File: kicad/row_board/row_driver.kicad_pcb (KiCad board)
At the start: 2 copper layers, 100 x 100 mm, 86 parts, among them J1 Panel row connector (female), J2 Row daisy chain connector (ma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, J3 Conn_01x04, J4 Conn_02x05_Odd_Even, J5 Conn_01x10, J6 Barrel_Jack, Q1 2N3904, U1 TPIC6B595, U10 TXB0108-PWR, U11 AdafruitProTrinket5V, U2 TPIC6B595, U3 TBD62783, U4 TPIC6B595, U5 TPIC6B595, U6 TBD62783, U7 WE-FDSM_DC/DC_5V, U8 4N25, U9 WeMos_mini

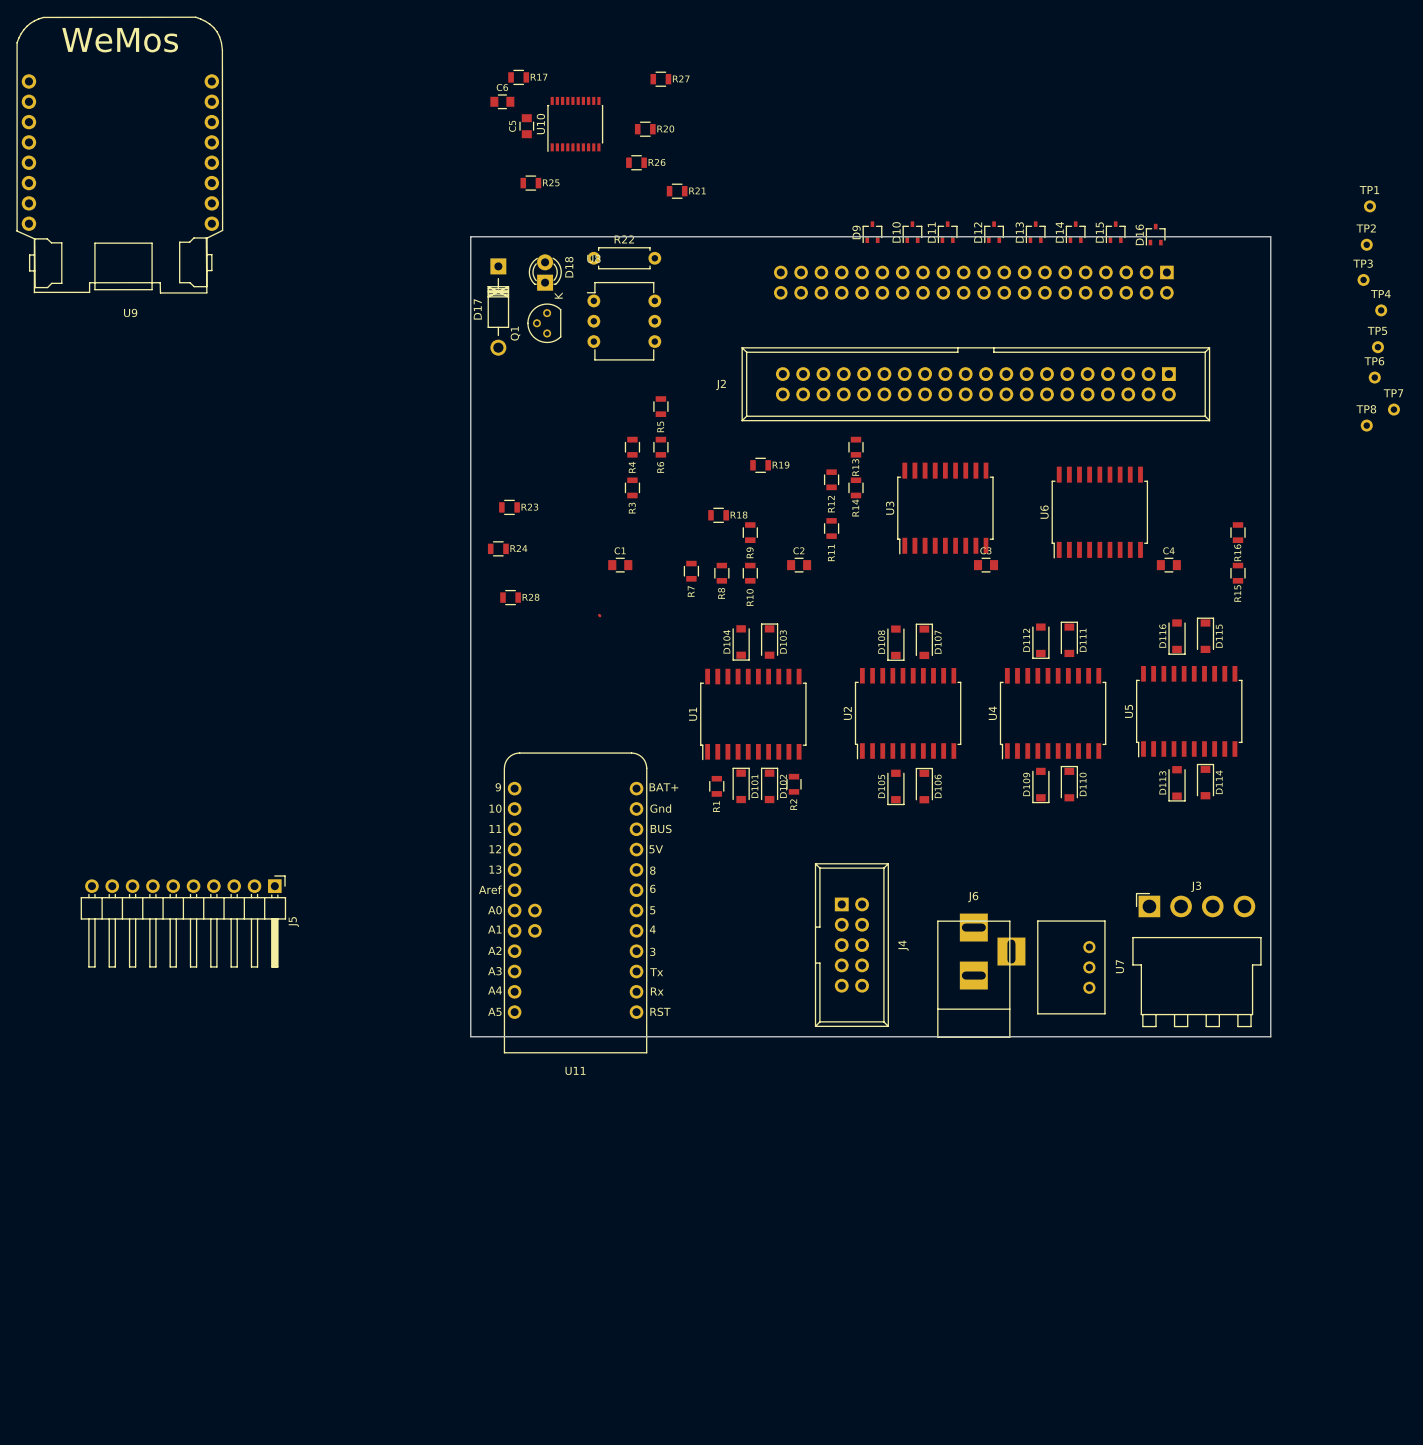
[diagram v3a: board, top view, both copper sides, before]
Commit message: Combine two controllers
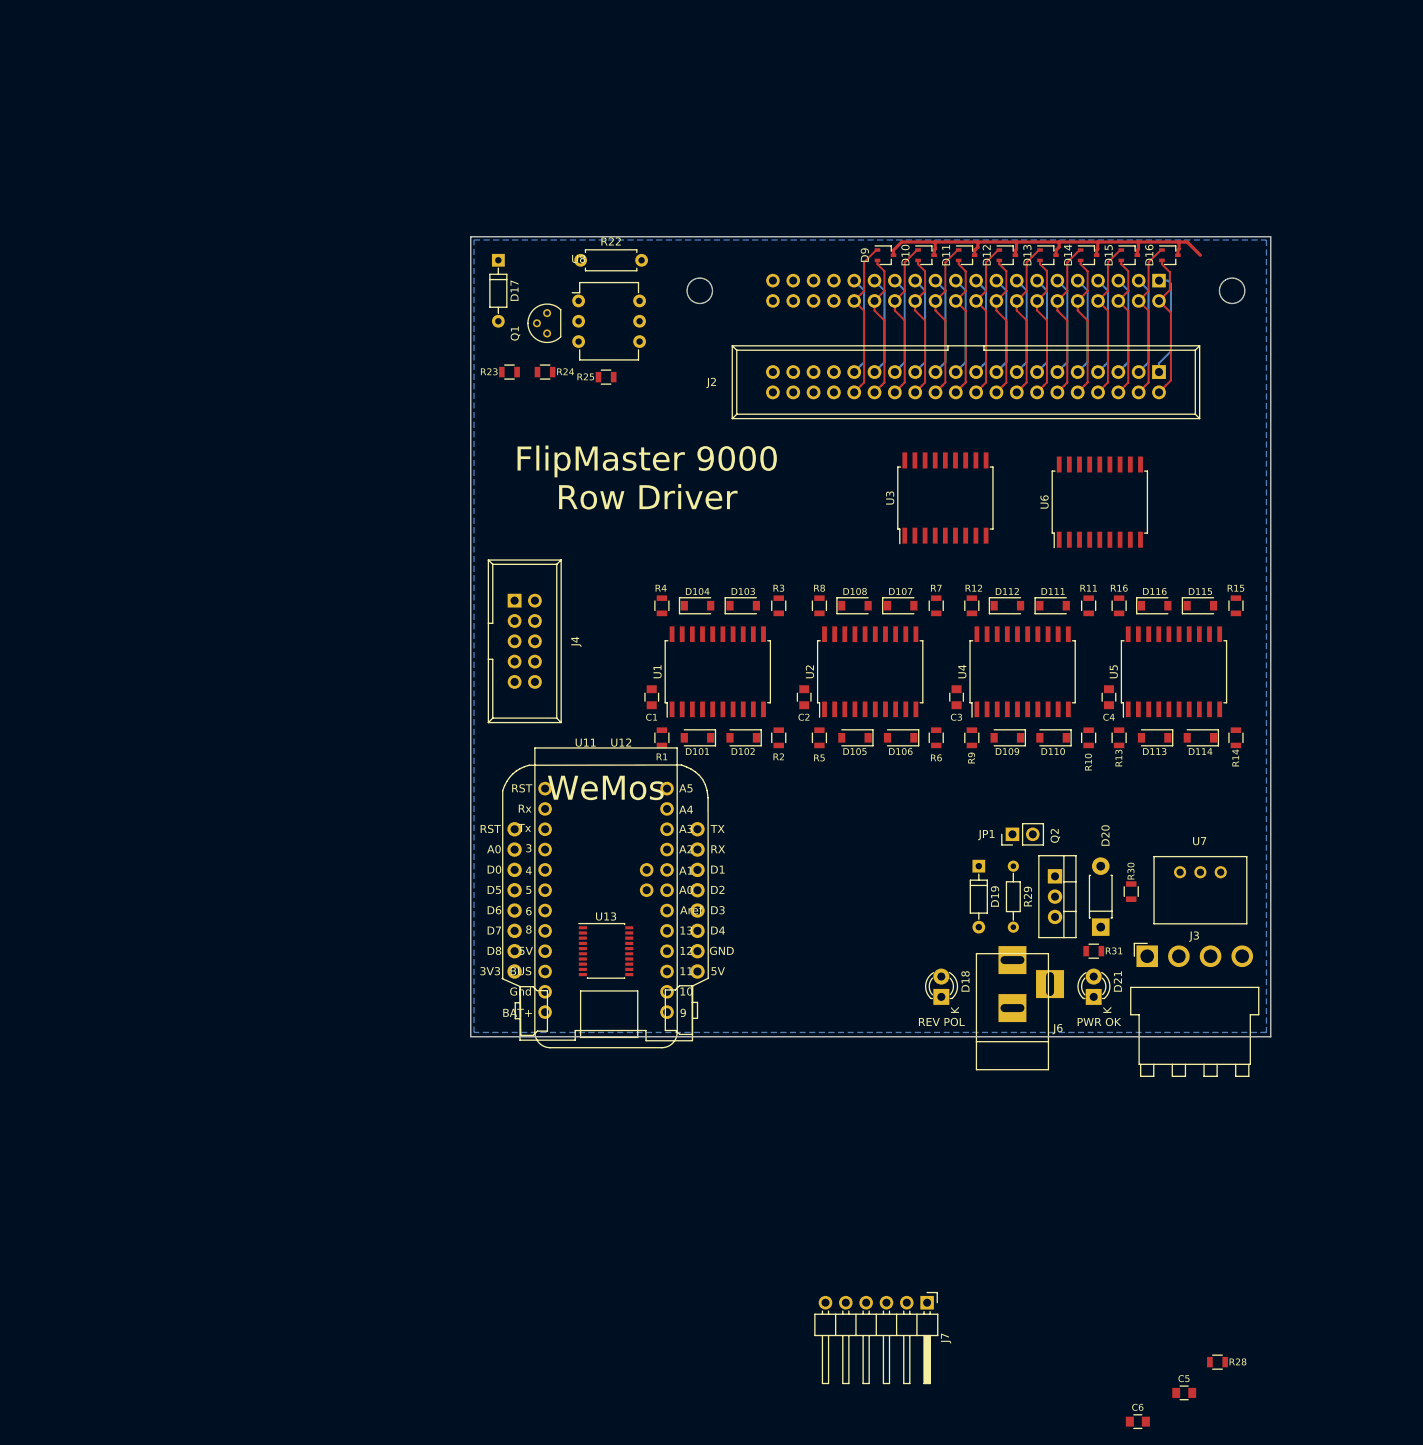
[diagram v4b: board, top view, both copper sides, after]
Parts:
- removed J5: Conn_01x10, Pin_Headers:Pin_Header_Angled_1x10_Pitch2.54mm
- removed R17, R18, R19, R20, R26, R27: 68K, lib_fp:R_0805
- removed R21: 10K, lib_fp:R_0805
- removed TP1, TP2, TP3, TP4, TP5, TP6, TP7, TP8: TEST_1P, Measurement_Points:Measurement_Point_Round-TH_Small
- removed U10: TXB0108-PWR, Housings_SSOP:SSOP-20_4.4x6.5mm_Pitch0.65mm
- removed U9: WeMos_mini, wemos_d1_mini:D1_mini_can_up
- added D19: 1N4148, Diodes_THT:D_DO-35_SOD27_P7.62mm_Horizontal, F.Cu at (88.5, 103.7)
- added D20: 1N4742, Diodes_THT:D_DO-41_SOD81_P7.62mm_Horizontal, F.Cu at (103.7, 111.3)
- added D21: LED, LEDs:LED-3MM, F.Cu at (102.9, 120.0)
- added J7: Conn_01x06, Pin_Headers:Pin_Header_Angled_1x06_Pitch2.54mm, F.Cu at (82.0, 158.2)
- added JP1: Jumper, Pin_Headers:Pin_Header_Straight_1x02_Pitch2.54mm, F.Cu at (92.7, 99.7)
- added Q2: FQP47P06, TO_SOT_Packages_THT:TO-220_Vertical, F.Cu at (98.0, 104.9)
- added R29: 2K7, Resistors_THT:R_Axial_DIN0204_L3.6mm_D1.6mm_P7.62mm_Horizontal, F.Cu at (92.8, 103.7)
- added R30: 2K7, lib_fp:R_0805, F.Cu at (107.6, 106.8)
- added R31: 470, lib_fp:R_0805, F.Cu at (102.9, 114.3)
- added U12: WeMos_mini, wemos_d1_mini:D1_mini_can_up, F.Cu at (41.9, 109.2)
- added U13: TXB0108-PWR, Housings_SSOP:SSOP-20_4.4x6.5mm_Pitch0.65mm, F.Cu at (41.9, 114.3)
- D17: value D -> 1N4148; footprint Diodes_THT:Diode_DO-41_SOD81_Horizontal_RM10 -> Diodes_THT:D_DO-35_SOD27_P7.62mm_Horizontal
- J1: footprint Socket_Strips:Socket_Strip_Straight_2x20_Pitch2.54mm -> lib_fp:Socket_Strip_Straight_2x20_Pitch2.54mm
- R23: value 4K7 -> 1K
- R28: value 2K7 -> 470
- moved C6 183.1 mm to (108.4, 173.1)
- moved C5 178.4 mm to (114.2, 169.5), turned to 0 degrees
- moved R28 130.2 mm to (118.3, 165.7)
- moved D18 102.1 mm to (83.8, 120.0)
- moved R14 56.9 mm to (120.7, 87.6)
- moved J4 55.8 mm to (30.5, 70.5)
- moved R6 50.0 mm to (83.2, 87.6)
- moved R13 49.0 mm to (106.0, 87.6)
- moved R10 47.0 mm to (102.2, 87.6)
- moved R5 45.9 mm to (68.6, 87.6)
- moved R9 37.7 mm to (87.6, 87.6)
- moved R11 33.5 mm to (102.2, 71.1)
- moved R7 30.9 mm to (83.2, 71.1)
- moved R25 26.0 mm to (41.9, 42.5), turned to 180 degrees
- moved J1 25.2 mm to (86.9, 31.8), turned to 0 degrees
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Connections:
- D18 pad 2: Net-(D18-Pad2) -> GND
- J3 pad 3: Net-(J3-Pad3) -> +24V
- J4 pad 5: COL_SR_CLK -> RC_SHIFT_CLK
- J4 pad 7: RC_REG_CLK -> COL_REG_CLK
- J4 pad 9: ~RC_CLR -> ~RC_CLEAR
- J6 pad 1: +24V -> Net-(J6-Pad1)
- Q1 pad 3: Net-(D18-Pad1) -> Net-(Q1-Pad3)
- R22 pad 2: ROW1_L -> ROW16_L
- R25 pad 1: +3V3 -> +5V
- U1 pad 12: RC_REG_CLK -> ROW_REG_CLK
- U1 pad 13: ROW_SR_CLK -> RC_SHIFT_CLK
- U1 pad 8: ~RC_CLR -> ~RC_CLEAR
- U11 pad 1: Net-(U11-Pad1) -> SENSE_EN
- U11 pad 10: Net-(U11-Pad10) -> CTRL3
- U11 pad 11: Net-(U11-Pad11) -> CTRL4
- U11 pad 12: Net-(U11-Pad12) -> CTRL5
- U11 pad 16: Net-(U11-Pad16) -> ~ROW_EN
- U11 pad 17: Net-(U11-Pad17) -> ROW_REG_CLK
- U11 pad 18: Net-(U11-Pad18) -> ~COL_EN
- U11 pad 19: Net-(U11-Pad19) -> COL_REG_CLK
- U11 pad 20: Net-(U11-Pad20) -> ~RC_CLEAR
- U11 pad 21: Net-(U11-Pad21) -> +5V
- U11 pad 23: Net-(U11-Pad23) -> GND
- U11 pad 3: Net-(U11-Pad3) -> RC_DATA
- U11 pad 4: Net-(U11-Pad4) -> ~SENSE
- U11 pad 5: Net-(U11-Pad5) -> RC_SHIFT_CLK
- U11 pad 7: Net-(U11-Pad7) -> CTRL0
- U11 pad 8: Net-(U11-Pad8) -> CTRL1
- U11 pad 9: Net-(U11-Pad9) -> CTRL2
- U2 pad 12: RC_REG_CLK -> ROW_REG_CLK
- U2 pad 13: ROW_SR_CLK -> RC_SHIFT_CLK
- U2 pad 8: ~RC_CLR -> ~RC_CLEAR
- U4 pad 12: RC_REG_CLK -> ROW_REG_CLK
- U4 pad 13: ROW_SR_CLK -> RC_SHIFT_CLK
- U4 pad 8: ~RC_CLR -> ~RC_CLEAR
- U5 pad 12: RC_REG_CLK -> ROW_REG_CLK
- U5 pad 13: ROW_SR_CLK -> RC_SHIFT_CLK
- U5 pad 8: ~RC_CLR -> ~RC_CLEAR
- U8 pad 2: Net-(D18-Pad2) -> Net-(Q1-Pad3)
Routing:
- net +24V: track 0.00 -> 52.3 mm
- net ROW14_L: track 0.00 -> 20.1 mm
- net ROW12_L: track 0.00 -> 20.1 mm
- net ROW10_L: track 0.00 -> 20.1 mm
- net ROW16_L: track 0.00 -> 20.1 mm
- net ROW8_L: track 0.00 -> 20.1 mm
- net ROW6_L: track 0.00 -> 20.1 mm
- net ROW4_L: track 0.00 -> 20.1 mm
- net ROW2_L: track 0.00 -> 20.1 mm
- net ROW1_L: track 0.00 -> 18.8 mm
- net ROW7_L: track 0.00 -> 18.4 mm
- net ROW5_L: track 0.00 -> 18.4 mm
- net ROW3_L: track 0.00 -> 18.4 mm
- net ROW15_L: track 0.00 -> 18.4 mm
- net ROW9_L: track 0.00 -> 18.4 mm
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- added copper zone on B.Cu, net GND
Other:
- net class High Current: trace_width 0.35 -> 0.4; via_dia 1.2 -> 1.5; via_drill 0.7 -> 0.75
- rule trace_min: 0.127 -> 0.09
- rule via_min_drill: 0.3 -> 0.2
- rule via_min_size: 0.6 -> 0.45
- board text added: "FlipMaster 9000 Row Driver"
- board text added: "PWR OK"
- board text added: "REV POL"

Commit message: Routed shift registers and row connectors
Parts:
- C5, C6, U13: moved to B.Cu
- U12: footprint wemos_d1_mini:D1_mini_can_up -> lib_fp:D1_mini_can_up
- moved C5 103.6 mm to (31.8, 106.7), turned to 180 degrees
- moved C6 99.8 mm to (31.8, 109.2)
- moved R28 51.3 mm to (77.1, 135.2)
- moved J7 38.6 mm to (78.0, 119.9)
- moved J4 12.8 mm to (32.3, 83.2), turned to 90 degrees
- moved U7 8.28 mm to (115.6, 98.4)
- moved R23 8.14 mm to (34.9, 48.3), turned to 0 degrees
- moved U13 7.41 mm to (38.1, 108.0), turned to 270 degrees
- moved R25 5.75 mm to (42.5, 48.3)
- moved Q1 4.87 mm to (35.2, 41.9)
- moved U8 4.87 mm to (39.1, 37.8)
- moved D17 4.51 mm to (29.2, 32.4)
- moved R22 4.46 mm to (39.1, 32.4)
- moved J3 3.81 mm to (109.6, 111.1)
- moved R24 3.24 mm to (34.9, 45.1)
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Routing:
- net +5V: track 0.00 -> 264.3 mm, vias 0 -> 9
- net +24V: track 52.3 -> 172.9 mm, vias 0 -> 3
- net ~RC_CLEAR: track 0.00 -> 99.1 mm, vias 0 -> 8
- net ROW_REG_CLK: track 0.00 -> 87.9 mm, vias 0 -> 6
- net ~ROW_EN: track 0.00 -> 85.3 mm
- net RC_SHIFT_CLK: track 0.00 -> 82.4 mm
- net Net-(D102-Pad2): track 0.00 -> 75.4 mm, vias 0 -> 2
- net ROW16_L: track 20.1 -> 94.1 mm, vias 0 -> 2
- net ROW11_L: track 18.4 -> 79.9 mm, vias 0 -> 4
- net ROW15_L: track 18.4 -> 78.7 mm, vias 0 -> 2
- net ROW13_L: track 18.4 -> 77.2 mm, vias 0 -> 2
- net Net-(D101-Pad2): track 0.00 -> 54.1 mm, vias 0 -> 2
- net Net-(D104-Pad2): track 0.00 -> 50.8 mm
- net ROW3_L: track 18.4 -> 68.8 mm, vias 0 -> 2
- net ROW4_L: track 20.1 -> 68.6 mm, vias 0 -> 2
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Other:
- net class Default: via_dia 1 -> 0.5; via_drill 0.5 -> 0.3
- net class High Current: via_dia 1.5 -> 0.8; via_drill 0.75 -> 0.5
- net class Power added: clearance 0.25, trace_width 0.65, via_dia 1, via_drill 0.75

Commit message: Routed all but controllers
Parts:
- added J8: Controller B, Connectors:IDC_Header_Straight_10pins, F.Cu at (85.8, 97.2)
- J4: value Conn_02x05_Odd_Even -> Column Board Connector
- J7: value Conn_01x06 -> Controller A; footprint Pin_Headers:Pin_Header_Angled_1x06_Pitch2.54mm -> Connectors:IDC_Header_Straight_10pins
- Q2: footprint TO_SOT_Packages_THT:TO-220_Vertical -> TO_SOT_Packages_THT:TO-220_Horizontal
- U11: value AdafruitProTrinket5V -> ArduinoNanoR3; footprint lib_fp:Adafruit_Trinket_Pro -> lib_fp:Arduino_Nano_R3
- moved R28 64.9 mm to (28.6, 92.1)
- moved D18 33.3 mm to (106.0, 95.2)
- moved J7 22.8 mm to (75.6, 97.2)
- moved D19 16.6 mm to (101.0, 92.7)
- moved R29 11.6 mm to (96.5, 92.7)
- moved JP1 10.8 mm to (99.7, 108.0), turned to 0 degrees
- moved D20 7.88 mm to (95.9, 111.8)
- moved J4 7.62 mm to (32.4, 75.6)
- moved R30 6.26 mm to (105.4, 101.0), turned to 180 degrees
- moved Q2 5.34 mm to (103.4, 105.4)
- moved J3 5.08 mm to (109.6, 116.2)
- moved C5 4.67 mm to (36.4, 106.0)
- moved C6 4.67 mm to (36.4, 108.6)
- moved U13 4.67 mm to (42.7, 107.3)
- moved U11 3.13 mm to (47.8, 107.3)
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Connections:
- net RC_DATA_OUT renamed Net-(U5-Pad18)
- J7 pad 1: CTRL5 -> CTRL_A0
- J7 pad 2: CTRL4 -> GND
- J7 pad 3: CTRL3 -> CTRL_A1
- J7 pad 4: CTRL2 -> GND
- J7 pad 5: CTRL1 -> CTRL_A2
- J7 pad 6: CTRL0 -> GND
- U11 pad 1: SENSE_EN -> RC_SHIFT_CLK
- U11 pad 10: CTRL3 -> CTRL_A4
- U11 pad 11: CTRL4 -> CTRL_B4
- U11 pad 12: CTRL5 -> +5V
- U11 pad 14: Net-(U11-Pad14) -> GND
- U11 pad 16: ~ROW_EN -> Net-(U11-Pad16)
- U11 pad 17: ROW_REG_CLK -> Net-(U11-Pad17)
- U11 pad 18: ~COL_EN -> Net-(U11-Pad18)
- U11 pad 19: COL_REG_CLK -> GND
- U11 pad 20: ~RC_CLEAR -> CTRL_B0
- U11 pad 21: +5V -> CTRL_A0
- U11 pad 22: Net-(U11-Pad22) -> ~ROW_EN
- U11 pad 23: GND -> ROW_REG_CLK
- U11 pad 24: Net-(U11-Pad24) -> ~COL_EN
- U11 pad 3: RC_DATA -> Net-(U11-Pad3)
- U11 pad 4: ~SENSE -> CTRL_A1
- U11 pad 5: RC_SHIFT_CLK -> CTRL_B1
- U11 pad 6: Net-(U11-Pad6) -> CTRL_A2
- U11 pad 7: CTRL0 -> CTRL_B2
- U11 pad 8: CTRL1 -> CTRL_A3
- U11 pad 9: CTRL2 -> CTRL_B3
- U12 pad 12: ~COL_EN_3v3 -> ROW_REG_CLK_3v3
- U12 pad 13: COL_REG_CLK_3v3 -> ~COL_EN_3v3
- U12 pad 14: ROW_REG_CLK_3v3 -> COL_REG_CLK_3v3
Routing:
- net +24V: track 172.9 -> 222.2 mm
- net +5V: track 264.3 -> 292.7 mm
- net Net-(J6-Pad1): track 0.00 -> 25.4 mm
- net Net-(D20-Pad2): track 0.00 -> 13.3 mm
- net Net-(D18-Pad1): track 0.00 -> 8.00 mm
- net Net-(D19-Pad1): track 0.00 -> 4.45 mm
- net Net-(D21-Pad2): track 0.00 -> 3.57 mm
- net GND: track 30.2 -> 33.0 mm, vias 18 -> 19
- net ROW13_L: track 77.2 -> 75.3 mm
- net ROW9_L: track 64.5 -> 63.9 mm
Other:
- net class PowerBus added: clearance 0.25, trace_width 1, via_dia 1.2, via_drill 0.75
- board text added: "+24V CTR POS"
- board text added: "CONT. A"
- board text added: "CONT. B"
- board text added: "Rev. 1.0 June, 2018"

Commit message: Finished routing row board; cleaning up.
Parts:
- C5, C6, U13: moved to F.Cu
- moved R28 9.13 mm to (37.6, 91.0)
- moved J4 8.03 mm to (29.8, 67.9), turned to 270 degrees
- moved C6 7.21 mm to (43.2, 106.1), turned to 90 degrees
- moved C5 6.30 mm to (30.1, 106.1), turned to 270 degrees
- moved U13 6.05 mm to (36.7, 107.4), turned to 0 degrees
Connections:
- J4 pad 3: RC_DATA -> RC_SHIFT_CLK
- J4 pad 5: RC_SHIFT_CLK -> ~RC_CLEAR
- J4 pad 7: COL_REG_CLK -> RC_DATA
- J4 pad 9: ~RC_CLEAR -> COL_REG_CLK
- U11 pad 22: ~ROW_EN -> COL_REG_CLK
- U11 pad 25: COL_REG_CLK -> ~ROW_EN
- U12 pad 3: ~SENSE_3v3 -> RC_SHIFT_CLK_3v3
- U12 pad 4: RC_SHIFT_CLK_3v3 -> ~SENSE_3v3
- U13 pad 1: ~ROW_EN_3v3 -> RC_DATA_3v3
- U13 pad 12: ~SENSE -> ~ROW_EN
- U13 pad 13: ~RC_CLEAR -> ROW_REG_CLK
- U13 pad 14: COL_REG_CLK -> ~COL_EN
- U13 pad 15: ROW_REG_CLK -> COL_REG_CLK
- U13 pad 17: RC_DATA -> ~SENSE
- U13 pad 18: ~COL_EN -> ~RC_CLEAR
- U13 pad 20: ~ROW_EN -> RC_DATA
- U13 pad 3: ~COL_EN_3v3 -> ~RC_CLR_3v3
- U13 pad 4: RC_DATA_3v3 -> ~SENSE_3v3
- U13 pad 6: ROW_REG_CLK_3v3 -> COL_REG_CLK_3v3
- U13 pad 7: COL_REG_CLK_3v3 -> ~COL_EN_3v3
- U13 pad 8: ~RC_CLR_3v3 -> ROW_REG_CLK_3v3
- U13 pad 9: ~SENSE_3v3 -> ~ROW_EN_3v3
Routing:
- net +5V: track 292.7 -> 391.3 mm, vias 9 -> 13
- net ~SENSE: track 10.0 -> 90.1 mm, vias 0 -> 2
- net RC_SHIFT_CLK: track 81.9 -> 161.8 mm, vias 0 -> 1
- net ~COL_EN: track 0.00 -> 60.9 mm, vias 0 -> 2
- net RC_DATA: track 11.6 -> 67.1 mm
- net ~RC_CLEAR: track 99.1 -> 153.1 mm
- net COL_REG_CLK: track 0.00 -> 53.9 mm, vias 0 -> 3
- net CTRL_B1: track 0.00 -> 51.9 mm
- net SENSE_EN_3v3: track 0.00 -> 49.7 mm, vias 0 -> 3
- net CTRL_B2: track 0.00 -> 45.8 mm
- net ROW_REG_CLK: track 87.9 -> 133.5 mm, vias 6 -> 8
- net CTRL_A1: track 0.00 -> 44.2 mm
- net CTRL_B3: track 0.00 -> 39.6 mm
- net CTRL_A2: track 0.00 -> 38.1 mm, vias 0 -> 1
- net CTRL_B4: track 0.00 -> 35.3 mm
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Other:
- board text added: "24VDC CTR+"
- board text added: "A"
- board text added: "B"
- board text added: "TO COL DRIVER"
- board text removed: "+24V CTR POS"
- board text removed: "CONT. A"
- board text removed: "CONT. B"
